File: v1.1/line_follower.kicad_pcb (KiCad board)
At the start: 2 copper layers, 60 x 80 mm, 32 parts, among them K1 BUZZER, P1 QTR-8A, P2 HC-05, P3 EXP HEADER, P4 LEFT MOTOR, P5 RIGHT MOTOR, P6 BATTERY, SW1 SW_PUSH, SW2 SW_PUSH, SW3 SW_PUSH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

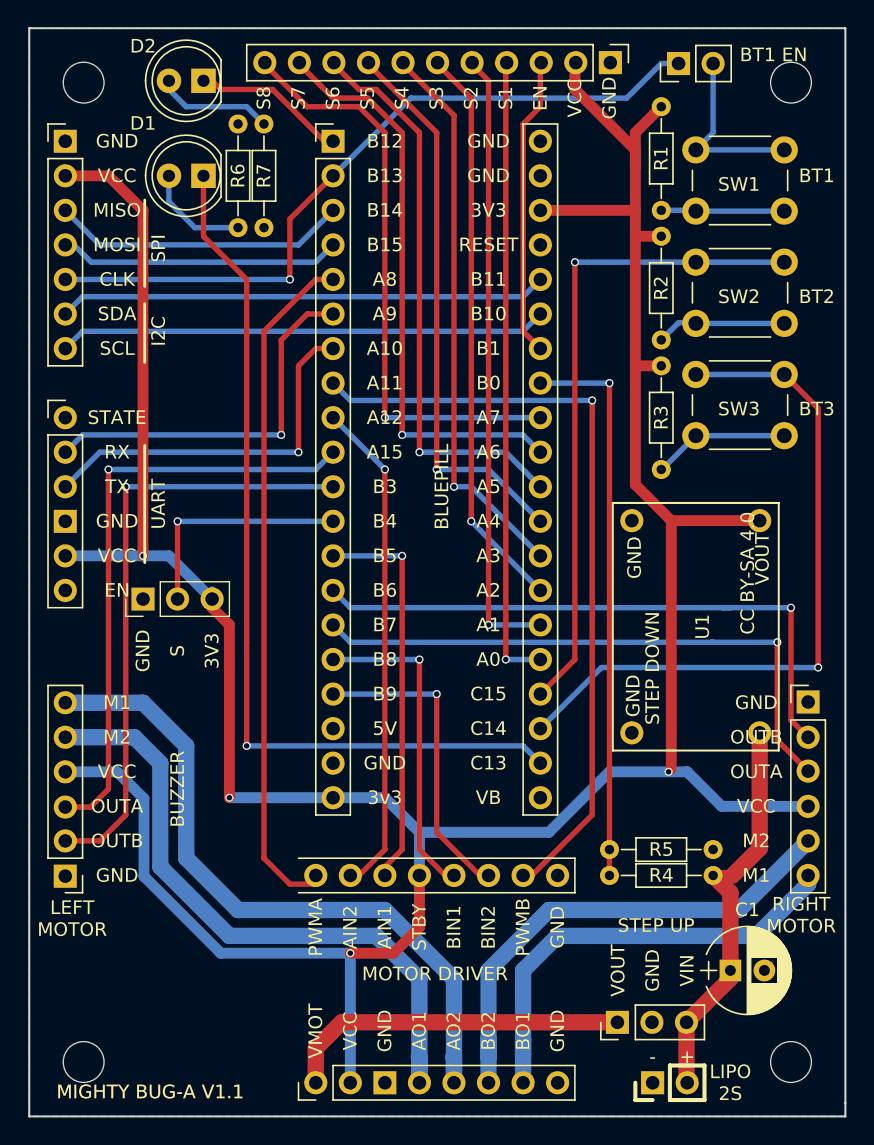
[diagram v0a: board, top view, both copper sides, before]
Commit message: Small cosmetic changes. Include schematic in PNG format.
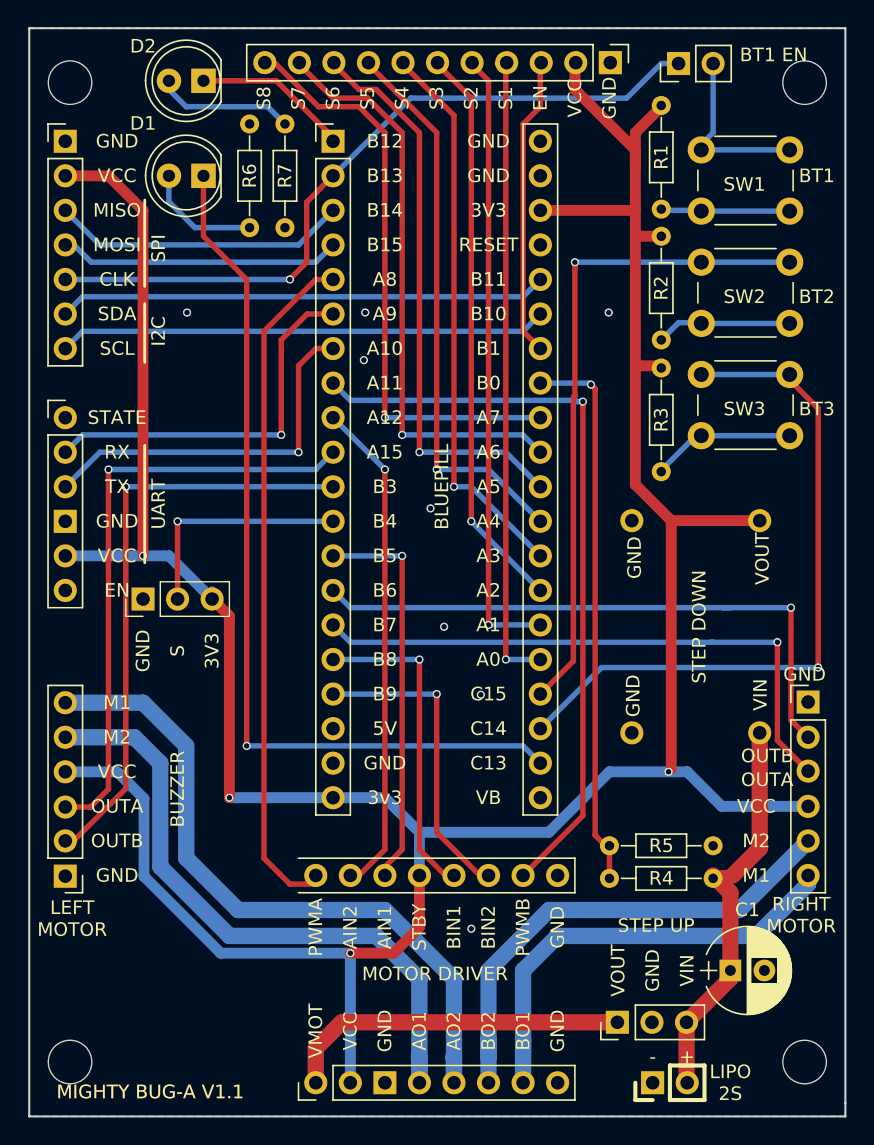
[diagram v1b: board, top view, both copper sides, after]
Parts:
- removed the G*** at (147.2, 91.0)
- removed Ref** (x4): MountingHole_3mm, line_follower:MountingHole_3mm
- added G***: LOGO, line_follower:testback, F.Cu at (147.9, 90.0)
- added REF**: MountingHole_3.2mm_M3, MountingHole:MountingHole_3.2mm_M3, F.Cu at (121.0, 135.0)
- added REF**: MountingHole_3.2mm_M3, MountingHole:MountingHole_3.2mm_M3, F.Cu at (175.0, 135.0)
- added REF**: MountingHole_3.2mm_M3, MountingHole:MountingHole_3.2mm_M3, F.Cu at (175.0, 63.0)
- added REF**: MountingHole_3.2mm_M3, MountingHole:MountingHole_3.2mm_M3, F.Cu at (121.0, 63.0)
- moved G*** 34.5 mm to (131.5, 133.5)
- moved G*** 22.9 mm to (161.0, 134.5)
- moved R7 1.55 mm to (136.8, 73.7)
- moved R6 0.85 mm to (134.2, 73.7)
- moved SW1 0.40 mm to (167.4, 67.9)
- moved SW2 0.40 mm to (167.4, 76.2)
- moved SW3 0.40 mm to (167.4, 84.5)
- moved R5 0.28 mm to (160.7, 119.1)
- moved R4 0.22 mm to (168.3, 121.5)
- moved R3 0.16 mm to (164.5, 91.6)
- moved R1 0.09 mm to (164.5, 72.3)
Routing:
- net RM_PWM: track 57.9 -> 55.6 mm
- net Net-(D2-Pad2): track 8.67 -> 10.2 mm
- net SENSOR8: track 44.0 -> 42.7 mm
- net LM_OUT_B: track 44.6 -> 43.5 mm
- net BAT_MEAS: track 41.3 -> 40.4 mm
- net Net-(D1-Pad2): track 7.77 -> 8.62 mm
- net GND: vias 0 -> 8
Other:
- board text removed: "CC BY-SA 4.0"
